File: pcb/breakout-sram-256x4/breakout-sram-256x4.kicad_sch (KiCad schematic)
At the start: 6 parts, among them J1 FX18-120P-0.8SV20, J2 FX18-120S-0.8SV20, U1 IS61WV102416DBLL-10TLI

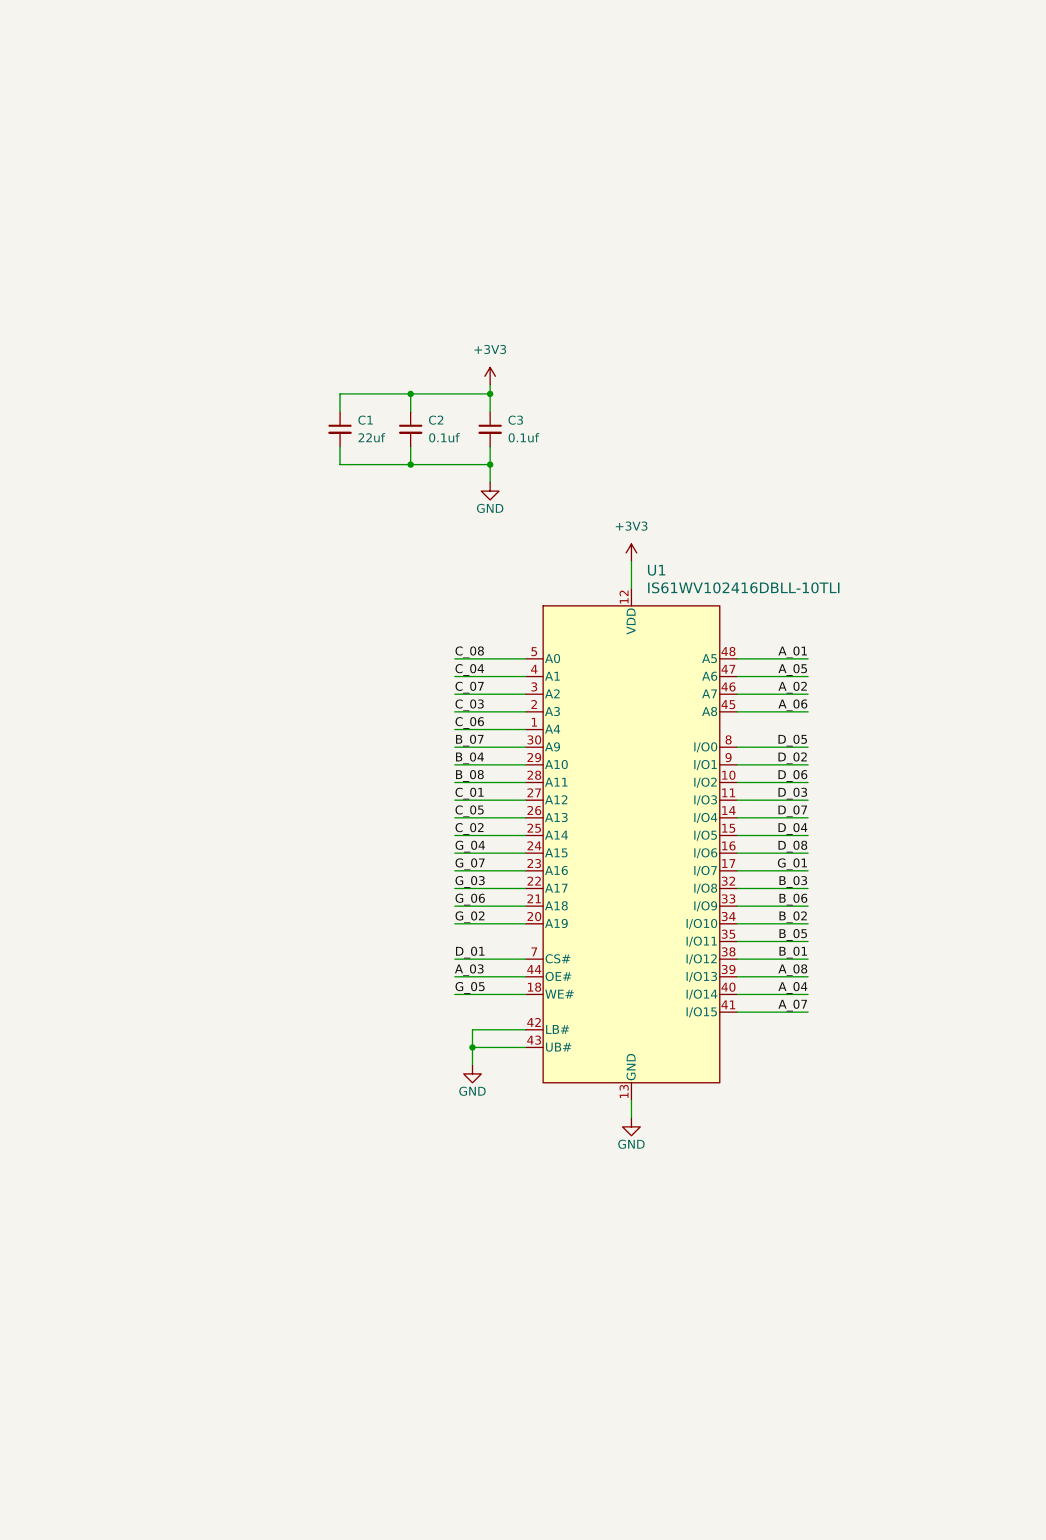
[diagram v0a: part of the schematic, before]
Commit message: [sram][pcb] standardize symbol and x4
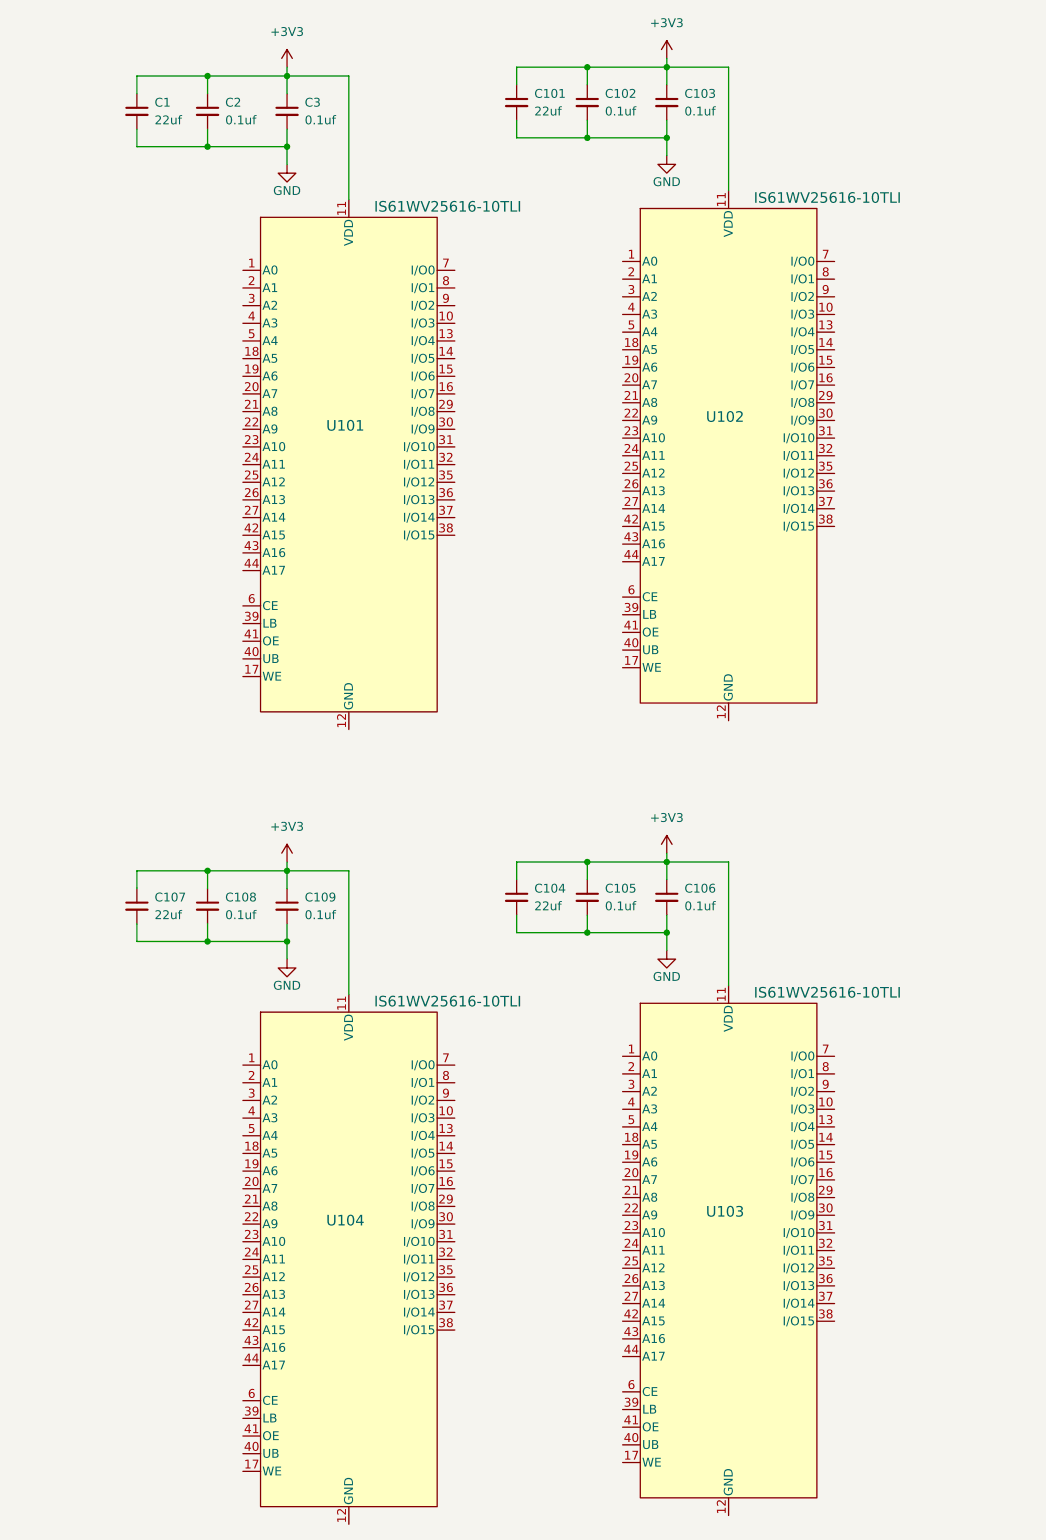
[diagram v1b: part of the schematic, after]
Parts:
- removed U1: IS61WV102416DBLL-10TLI, IS61WV102416DBLL-10TLI_ISI, symbol IS61WV102416DBLL-10TLI:IS61WV102416DBLL-10TLI
- added C101, C104, C107: 22uf, Capacitor_SMD:C_0603_1608Metric, symbol Device:C_Small
- added C102, C103, C105, C106, C108, C109: 0.1uf, Capacitor_SMD:C_0402_1005Metric, symbol Device:C_Small
- added U101, U102, U103, U104: IS61WV25616-10TLI, 44L_TSOP-2_400_ISI, symbol IS61WV25616-10TLI:IS61WV25616BLL-10TLI-TR
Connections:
- net +3V3: now also C101.1, C102.1, C103.1, C104.1, C105.1, C106.1, C107.1, C108.1, C109.1, U101.11 (VDD), U101.33 (VDD), U102.11 (VDD), U102.33 (VDD), U103.11 (VDD), U103.33 (VDD), U104.11 (VDD), U104.33 (VDD)
- net GND: now also C101.2, C102.2, C103.2, C104.2, C105.2, C106.2, C107.2, C108.2, C109.2
- new net: U103.12 (GND), U103.34 (GND)
- new net: U101.12 (GND), U101.34 (GND)
- new net: U102.12 (GND), U102.34 (GND)
- new net: U104.12 (GND), U104.34 (GND)
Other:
- moved on the sheet: C1, C2, C3

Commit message: [sram][pcb] add footprint for 256x4
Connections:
- net GND: now also U101.12 (GND), U101.34 (GND), U102.12 (GND), U102.34 (GND), U103.12 (GND), U103.34 (GND), U104.12 (GND), U104.34 (GND)
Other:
- moved on the sheet: C1, C101, C102, C103, C104, C105, C106, C107, C108, C109, C2, C3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

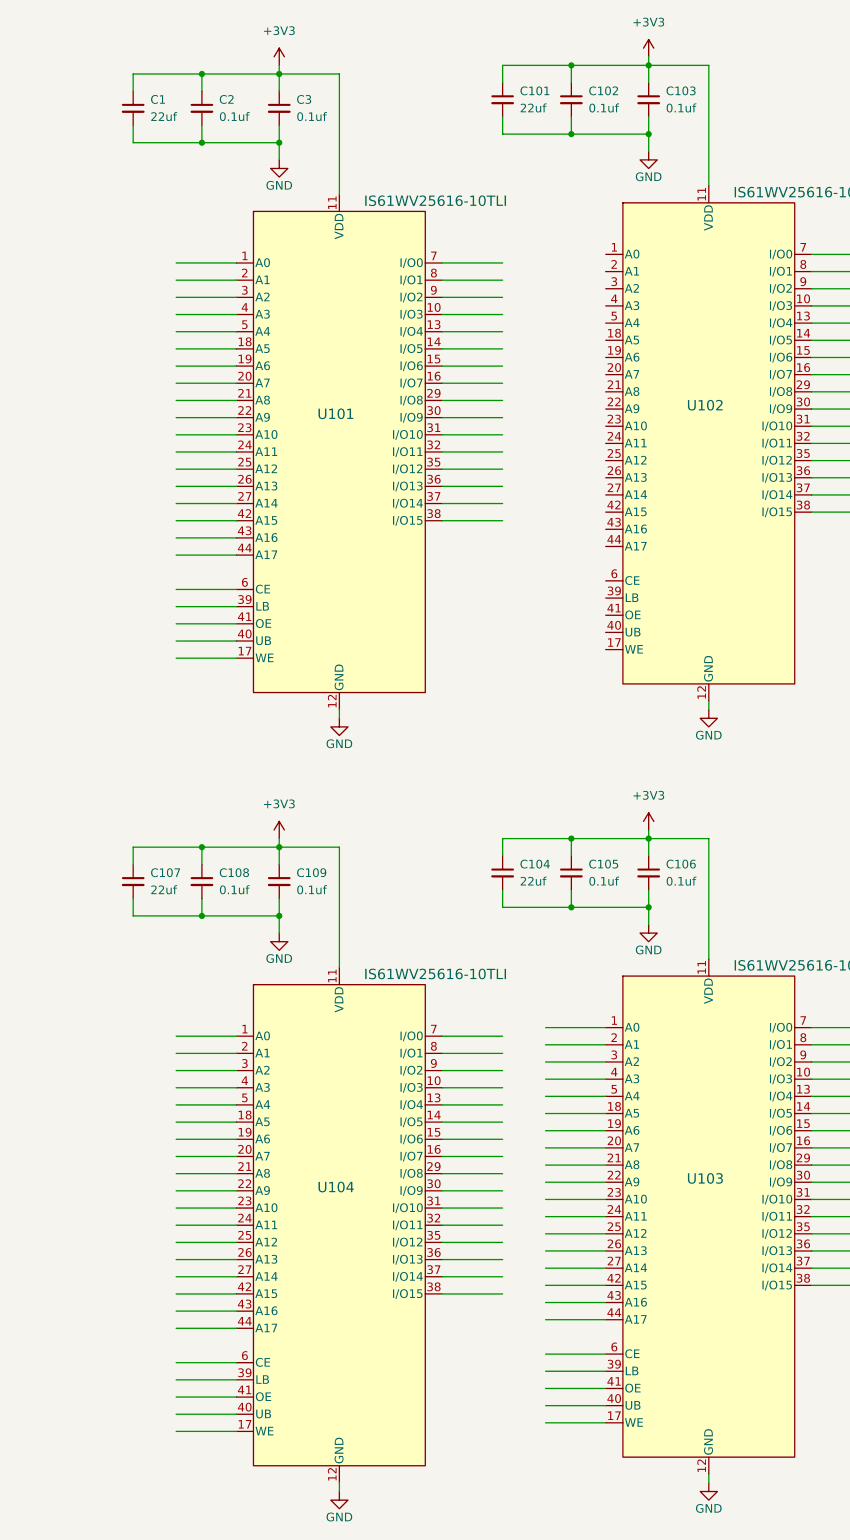
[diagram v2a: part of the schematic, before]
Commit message: [sram][pcb] rough footprint placement
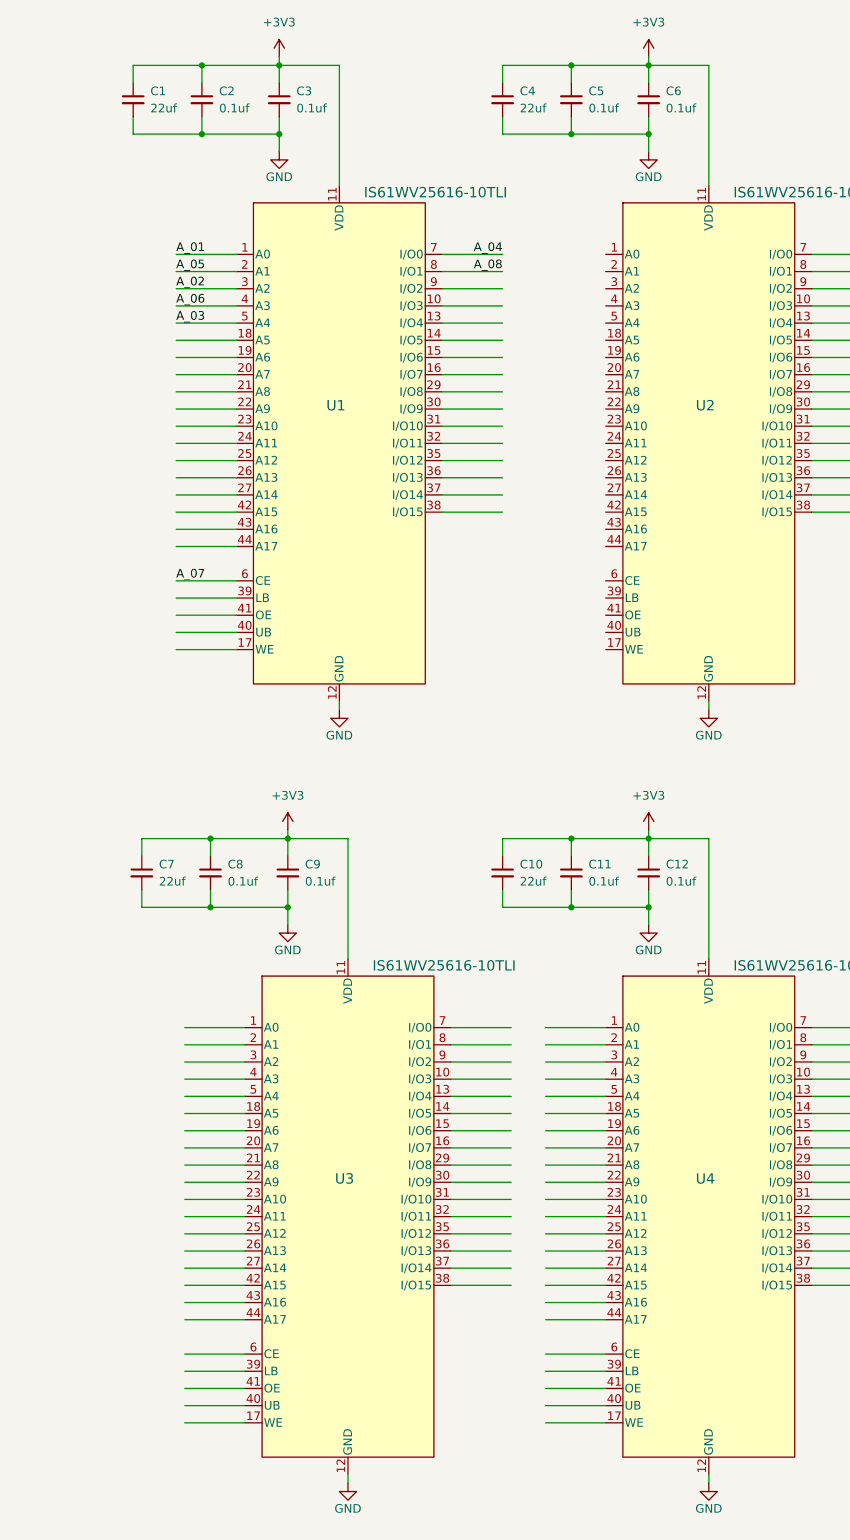
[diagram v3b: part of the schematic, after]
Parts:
- renumbered C104 to C10, C105 to C11, C106 to C12, C101 to C4, C102 to C5, C103 to C6, C107 to C7, C108 to C8, C109 to C9, U101 to U1, U102 to U2, U104 to U3, U103 to U4
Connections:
- net A_01: now also U1.1 (A0)
- net A_02: now also U1.3 (A2)
- net A_03: now also U1.5 (A4)
- net A_04: now also U1.7 (I/O0)
- net A_05: now also U1.2 (A1)
- net A_06: now also U1.4 (A3)
- net A_07: now also U1.6 (CE)
- net A_08: now also U1.8 (I/O1)
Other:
- moved on the sheet: C1, C2, C3, C7, C8, C9, U1, U3

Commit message: [sram][pcb] reduce to 2x and partial routing:
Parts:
- removed C10, C4: 22uf, Capacitor_SMD:C_0603_1608Metric, symbol Device:C_Small
- removed C11, C12, C5, C6: 0.1uf, Capacitor_SMD:C_0402_1005Metric, symbol Device:C_Small
- removed U2, U4: IS61WV25616-10TLI, 44L_TSOP-2_400_ISI, symbol IS61WV25616-10TLI:IS61WV25616BLL-10TLI-TR
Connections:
- net B_01: now also U1.9 (I/O2)
- net B_02: now also U1.13 (I/O4)
- net B_03: now also U1.15 (I/O6)
- net B_04: now also U1.17 (WE)
- net B_05: now also U1.10 (I/O3)
- net B_06: now also U1.14 (I/O5)
- net B_07: now also U1.16 (I/O7)
- net B_08: now also U1.18 (A5)
- net C_01: now also U1.19 (A6)
- net C_02: now also U1.21 (A8)
- net C_03: now also U1.44 (A17)
- net C_04: now also U1.42 (A15)
- net C_05: now also U1.20 (A7)
- net C_06: now also U1.22 (A9)
- net C_07: now also U1.43 (A16)
- net C_08: now also U1.41 (OE)
- net D_01: now also U1.32 (I/O11)
- net D_02: now also U1.30 (I/O9)
- net D_05: now also U1.31 (I/O10)
- net D_06: now also U1.29 (I/O8)
- no-connect marks 41 -> 49
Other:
- note added: "avoid EFL"
